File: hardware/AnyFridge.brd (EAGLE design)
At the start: 75.9 x 69.8 mm, 11 parts

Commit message: Minor updates.
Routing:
- net RX1: track 57.2 -> 56.4 mm
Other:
- board text added: "Designed by: AnyFridge Team Ethan Anderson, Isac Fletcher, Caden Allen"
- board text removed: "Designed by: Ethan Anderson, Isaac Fletcher, Caden Allen"
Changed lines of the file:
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@@
 <text x="5.08" y="46.99" size="1.778" layer="21">RGB LED</text>
 <text x="63.5" y="53.34" size="1.778" layer="21">Mode Toggle</text>
-<text x="5.08" y="36.83" size="1.778" layer="21" rot="SR270">Designed by:
+<text x="10.16" y="29.21" size="1.524" layer="21" rot="SR270" align="center">Designed by:
+AnyFridge Team
 Ethan Anderson,
-Isaac Fletcher,
+Isac Fletcher,
 Caden Allen</text>
 <text x="54.61" y="60.96" size="1.778" layer="21" rot="R270">R1</text>
@@
 <attribute name="MF" value="Vishay" x="35.56" y="-148.59" size="1.778" layer="27" display="off"/>
 <attribute name="MP" value="TSSP77038TT" x="35.56" y="-148.59" size="1.778" layer="27" display="off"/>
+<attribute name="NAME" x="12.64" y="5.83" size="1" layer="25" ratio="20" rot="SR0"/>
 <attribute name="NAME" x="12.64" y="5.83" size="1" layer="51" ratio="21" rot="SR0"/>
-<attribute name="NAME" x="12.64" y="5.83" size="1" layer="25" ratio="20" rot="SR0"/>
 <attribute name="PACKAGE" value="None" x="35.56" y="-148.59" size="1.778" layer="27" display="off"/>
 <attribute name="PRICE" value="None" x="35.56" y="-148.59" size="1.778" layer="27" display="off"/>
@@
 <contactref element="SCAN-1" pad="TX"/>
 <wire x1="49.53" y1="35.56" x2="44.45" y2="40.64" width="0.4064" layer="1"/>
-<wire x1="44.45" y1="49.53" x2="44.45" y2="40.64" width="0.4064" layer="1"/>
-<wire x1="44.45" y1="49.53" x2="40.64" y2="49.53" width="0.4064" layer="1"/>
+<wire x1="44.45" y1="40.64" x2="44.45" y2="48.26" width="0.4064" layer="1"/>
+<wire x1="44.45" y1="48.26" x2="43.18" y2="49.53" width="0.4064" layer="1"/>
+<wire x1="43.18" y1="49.53" x2="40.64" y2="49.53" width="0.4064" layer="1"/>
 <contactref element="TP_RX" pad="TP"/>
 <wire x1="13.11185" y1="62.23" x2="11.84185" y2="63.5" width="0.4064" layer="16"/>

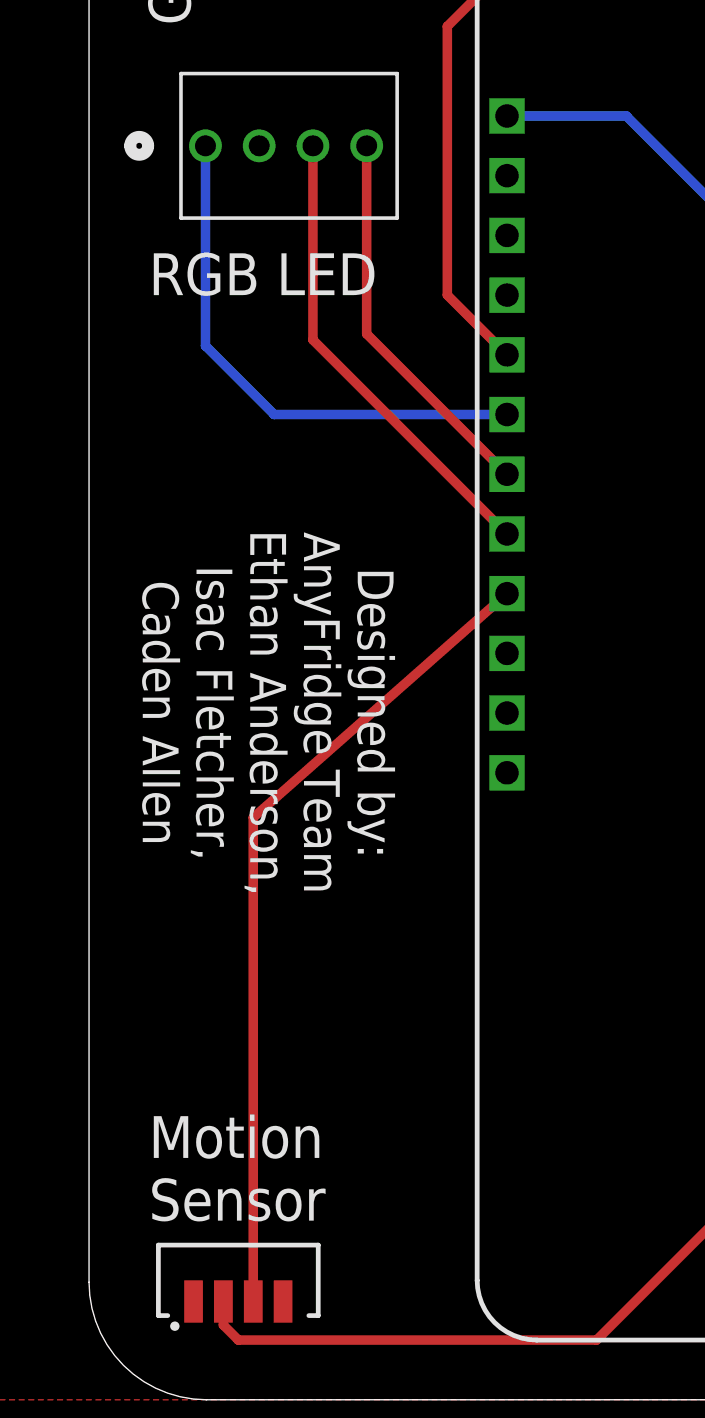
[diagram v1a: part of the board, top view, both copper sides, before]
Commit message: Added 120 ohm resistor to board/schematic
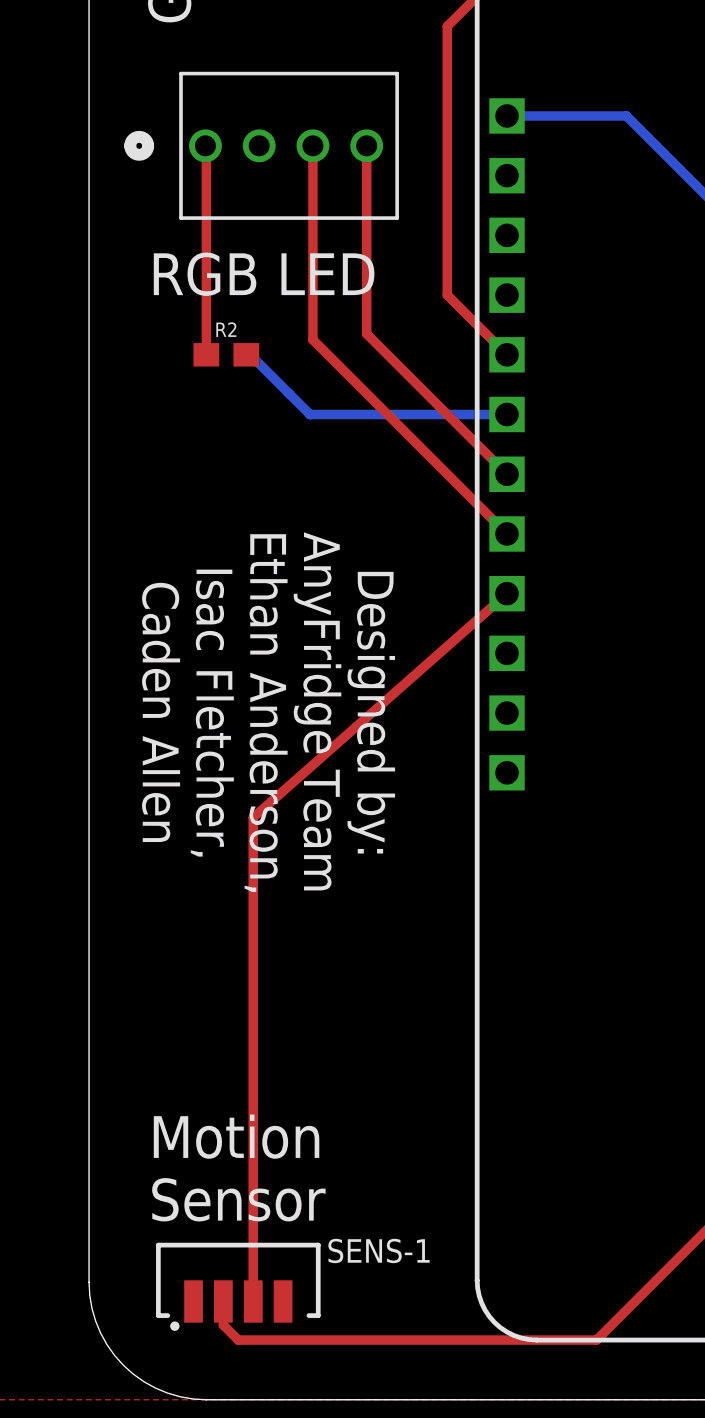
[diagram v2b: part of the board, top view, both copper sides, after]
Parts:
- added R2: 120OHM, SparkFun-Resistors:0603
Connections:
- removed net RED: ESP-1.33, LED-1.1
- new net RED-IN: ESP-1.33, R2.2
- new net RED-OUT: LED-1.1, R2.1
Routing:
- net RED: track 22.5 -> 0.00 mm
- net RED-IN: track 0.00 -> 12.5 mm
- net RED-OUT: track 0.00 -> 8.91 mm
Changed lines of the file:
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@@
 <layer number="154" name="FabDoc2" color="7" fill="1" visible="no" active="no"/>
 <layer number="155" name="FabDoc3" color="7" fill="1" visible="no" active="no"/>
+<layer number="156" name="gesam-Maß" color="1" fill="7" visible="no" active="no"/>
+<layer number="157" name="FaceMchng" color="3" fill="1" visible="no" active="no"/>
+<layer number="158" name="FaceMMeas" color="3" fill="1" visible="no" active="no"/>
+<layer number="159" name="Geh-Bear2" color="1" fill="7" visible="no" active="no"/>
+<layer number="160" name="Topologie" color="9" fill="1" visible="no" active="no"/>
+<layer number="161" name="tomplace2" color="7" fill="1" visible="no" active="no"/>
 <layer number="166" name="AntennaArea" color="7" fill="1" visible="no" active="no"/>
 <layer number="168" name="4mmHeightArea" color="7" fill="1" visible="no" active="no"/>
@@
 <layer number="250" name="Descript" color="3" fill="1" visible="no" active="no"/>
 <layer number="251" name="SMDround" color="12" fill="11" visible="no" active="no"/>
+<layer number="252" name="BR-BS" color="7" fill="1" visible="no" active="no"/>
 <layer number="253" name="Extra" color="7" fill="1" visible="no" active="no"/>
 <layer number="254" name="cooling" color="7" fill="1" visible="no" active="no"/>
@@
 <attribute name="MF" value="Vishay" x="35.56" y="-148.59" size="1.778" layer="27" display="off"/>
 <attribute name="MP" value="TSSP77038TT" x="35.56" y="-148.59" size="1.778" layer="27" display="off"/>
+<attribute name="NAME" x="12.64" y="5.83" size="1" layer="51" ratio="21" rot="SR0"/>
 <attribute name="NAME" x="12.64" y="5.83" size="1" layer="25" ratio="20" rot="SR0"/>
-<attribute name="NAME" x="12.64" y="5.83" size="1" layer="51" ratio="21" rot="SR0"/>
 <attribute name="PACKAGE" value="None" x="35.56" y="-148.59" size="1.778" layer="27" display="off"/>
 <attribute name="PRICE" value="None" x="35.56" y="-148.59" size="1.778" layer="27" display="off"/>
@@
 <attribute name="TP_SIGNAL_NAME" value="" x="13.97" y="66.04" size="1.778" layer="27" rot="R90" display="off"/>
 <attribute name="VALUE" x="10.16" y="64.77" size="0.0254" layer="27" rot="R90"/>
+</element>
+<element name="R2" library="SparkFun-Resistors" package="0603" value="120OHM" x="8.382" y="44.45" smashed="yes">
+<attribute name="NAME" x="8.382" y="45.212" size="0.6096" layer="25" font="vector" ratio="20" align="bottom-center"/>
+<attribute name="VALUE" x="8.382" y="43.688" size="0.6096" layer="27" font="vector" ratio="20" align="top-center"/>
 </element>
 </elements>
@@
 <wire x1="30.48" y1="20.32" x2="30.48" y2="49.53" width="0.4064" layer="16"/>
 </signal>
-<signal name="RED">
-<contactref element="LED-1" pad="1"/>
+<signal name="RED-IN">
 <contactref element="ESP-1" pad="33"/>
-<wire x1="10.414" y1="41.91" x2="20.32" y2="41.91" width="0.4064" layer="16"/>
-<wire x1="7.493" y1="44.831" x2="10.414" y2="41.91" width="0.4064" layer="16"/>
-<wire x1="7.493" y1="53.34" x2="7.493" y2="44.831" width="0.4064" layer="16"/>
+<wire x1="20.32" y1="41.91" x2="11.938" y2="41.91" width="0.4064" layer="16"/>
+<wire x1="11.938" y1="41.91" x2="11.049" y2="42.799" width="0.4064" layer="16"/>
+<contactref element="R2" pad="2"/>
+<wire x1="11.049" y1="42.799" x2="9.398" y2="44.45" width="0.4064" layer="16"/>
+<wire x1="9.398" y1="44.45" x2="8.89" y2="44.45" width="0.4064" layer="16"/>
+<wire x1="8.89" y1="44.45" x2="9.232" y2="44.45" width="0" layer="19" extent="1-16"/>
 </signal>
 <signal name="BLUE">
@@
 <wire x1="9.525" y1="24.765" x2="9.525" y2="4.18" width="0.4064" layer="1"/>
 </signal>
+<signal name="RED-OUT">
+<contactref element="LED-1" pad="1"/>
+<contactref element="R2" pad="1"/>
+<wire x1="7.532" y1="44.45" x2="7.532" y2="53.301" width="0.4064" layer="1"/>
+<wire x1="7.532" y1="53.301" x2="7.493" y2="53.34" width="0.4064" layer="1"/>
+</signal>
 </signals>

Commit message: schematic updated
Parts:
- R2: value 120OHM -> 68OHM-0603-1/10W-1%
- moved R2 0.76 mm to (7.62, 44.5)
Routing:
- net RED-IN: track 12.5 -> 12.9 mm, vias 0 -> 1
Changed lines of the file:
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@@
 <attribute name="VALUE" x="10.16" y="64.77" size="0.0254" layer="27" rot="R90"/>
 </element>
-<element name="R2" library="SparkFun-Resistors" package="0603" value="120OHM" x="8.382" y="44.45" smashed="yes">
-<attribute name="NAME" x="8.382" y="45.212" size="0.6096" layer="25" font="vector" ratio="20" align="bottom-center"/>
-<attribute name="VALUE" x="8.382" y="43.688" size="0.6096" layer="27" font="vector" ratio="20" align="top-center"/>
+<element name="R2" library="SparkFun-Resistors" package="0603" value="68OHM-0603-1/10W-1%" x="7.62" y="44.45" smashed="yes">
+<attribute name="NAME" x="7.62" y="45.212" size="0.6096" layer="25" font="vector" ratio="20" align="bottom-center"/>
+<attribute name="VALUE" x="7.62" y="43.688" size="0.6096" layer="27" font="vector" ratio="20" align="top-center"/>
 </element>
 </elements>
@@
 <contactref element="ESP-1" pad="33"/>
 <wire x1="20.32" y1="41.91" x2="11.938" y2="41.91" width="0.4064" layer="16"/>
-<wire x1="11.938" y1="41.91" x2="11.049" y2="42.799" width="0.4064" layer="16"/>
 <contactref element="R2" pad="2"/>
-<wire x1="11.049" y1="42.799" x2="9.398" y2="44.45" width="0.4064" layer="16"/>
-<wire x1="9.398" y1="44.45" x2="8.89" y2="44.45" width="0.4064" layer="16"/>
-<wire x1="8.89" y1="44.45" x2="9.232" y2="44.45" width="0" layer="19" extent="1-16"/>
+<via x="11.938" y="41.91" extent="1-16" drill="0.35"/>
+<wire x1="11.938" y1="41.91" x2="9.398" y2="44.45" width="0.4064" layer="1"/>
+<wire x1="9.398" y1="44.45" x2="8.47" y2="44.45" width="0.4064" layer="1"/>
 </signal>
 <signal name="BLUE">
@@
 <contactref element="LED-1" pad="1"/>
 <contactref element="R2" pad="1"/>
-<wire x1="7.532" y1="44.45" x2="7.532" y2="53.301" width="0.4064" layer="1"/>
-<wire x1="7.532" y1="53.301" x2="7.493" y2="53.34" width="0.4064" layer="1"/>
+<wire x1="6.77" y1="44.45" x2="6.77" y2="52.617" width="0.4064" layer="1"/>
+<wire x1="6.77" y1="52.617" x2="7.493" y2="53.34" width="0.4064" layer="1"/>
 </signal>
 </signals>

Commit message: Add Green and Blue resistors
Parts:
- added R3, R4: 22Ω, SparkFun-Resistors:0603
- moved R2 1.27 mm to (6.35, 44.5), turned to 270 degrees
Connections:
- net RED-IN renamed RED
- new net N$2: LED-1.4, R3.1
- new net N$3: LED-1.3, R4.1
- net BLUE: now also R4.2; no longer LED-1.3
- net GREEN: now also R3.2; no longer LED-1.4
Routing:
- net N$3: track 0.00 -> 8.83 mm
- net GREEN: track 16.4 -> 8.10 mm
- net N$2: track 0.00 -> 8.20 mm
- net BLUE: track 19.9 -> 14.7 mm
- net RED: track 12.9 -> 15.7 mm
- net RED-OUT: track 9.19 -> 8.51 mm
- net 3.3V: track 152.1 -> 152.6 mm
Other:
- board text added: "AnyFridge V1.0"
- board text added: "Designed by: Ethan Anderson, Isac Fletcher, Caden Allen"
- board text removed: "Designed by: AnyFridge Team Ethan Anderson, Isac Fletcher, Caden Allen"

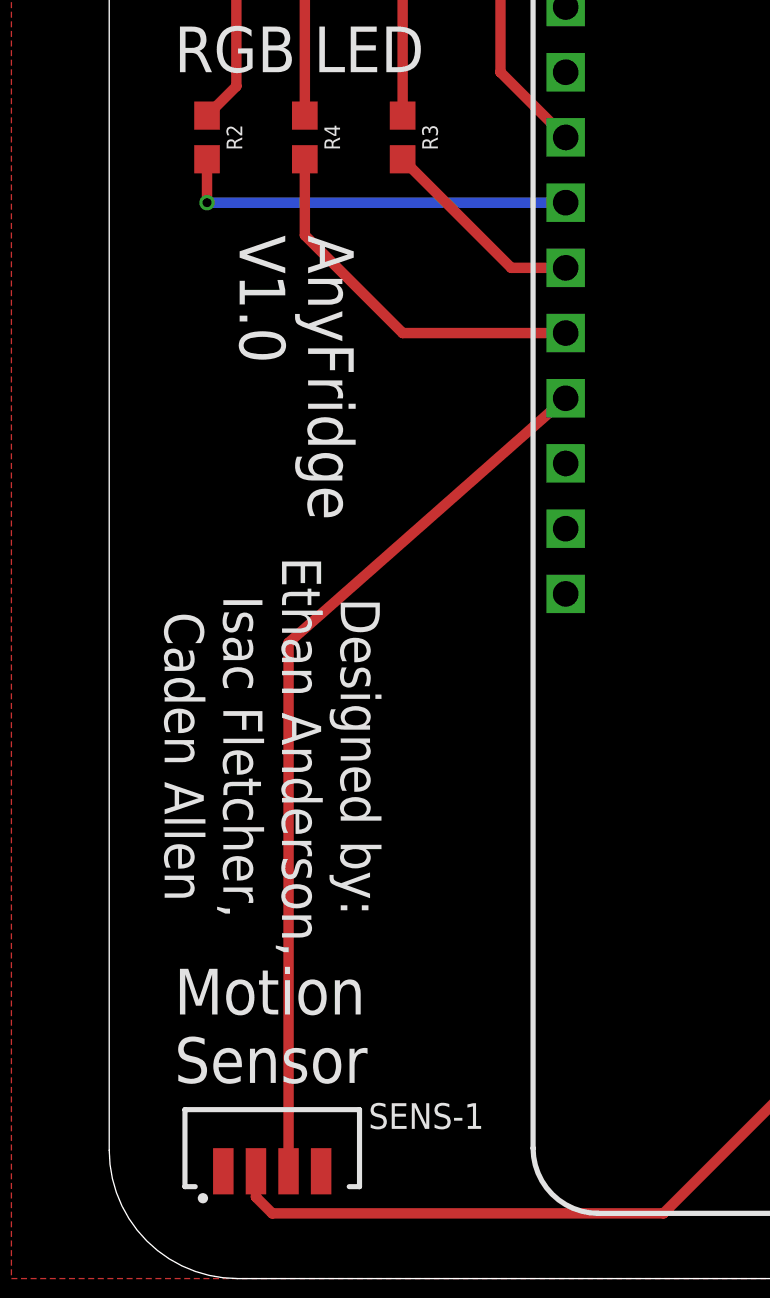
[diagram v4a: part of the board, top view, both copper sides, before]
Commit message: Put project name + revision in silkscreen, rename resistor to LED pins
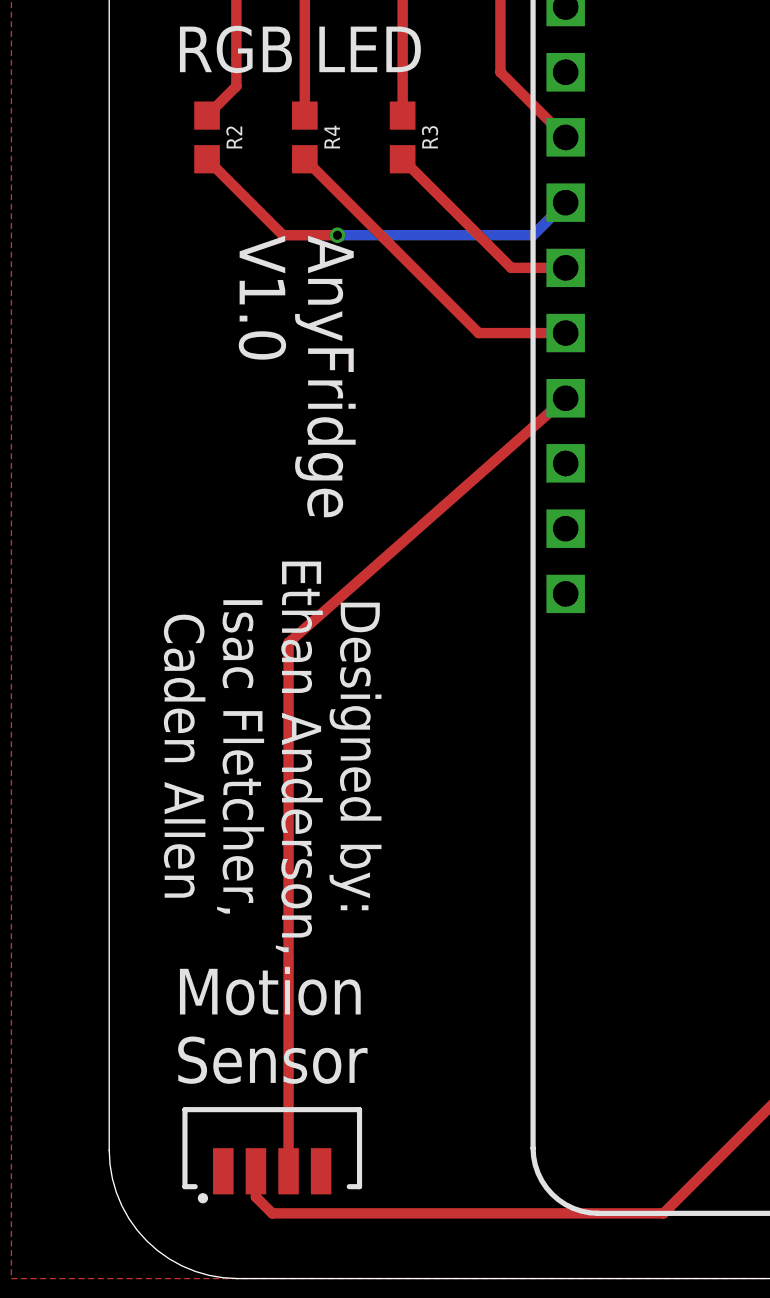
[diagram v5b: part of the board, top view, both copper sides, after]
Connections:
- net N$2 renamed GREEN-IN
- net N$3 renamed BLUE-IN
- net RED-OUT renamed RED-IN
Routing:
- net BLUE: track 14.7 -> 13.0 mm
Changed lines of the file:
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@@
 <attribute name="MF" value="Vishay" x="35.56" y="-148.59" size="1.778" layer="27" display="off"/>
 <attribute name="MP" value="TSSP77038TT" x="35.56" y="-148.59" size="1.778" layer="27" display="off"/>
+<attribute name="NAME" x="12.64" y="5.83" size="1" layer="25" ratio="20" rot="SR0"/>
 <attribute name="NAME" x="12.64" y="5.83" size="1" layer="51" ratio="21" rot="SR0"/>
-<attribute name="NAME" x="12.64" y="5.83" size="1" layer="25" ratio="20" rot="SR0"/>
 <attribute name="PACKAGE" value="None" x="35.56" y="-148.59" size="1.778" layer="27" display="off"/>
 <attribute name="PRICE" value="None" x="35.56" y="-148.59" size="1.778" layer="27" display="off"/>
@@
 <contactref element="ESP-1" pad="12"/>
 <contactref element="R4" pad="2"/>
-<wire x1="10.16" y1="43.6" x2="10.16" y2="40.64" width="0.4064" layer="1"/>
-<wire x1="10.16" y1="40.64" x2="13.97" y2="36.83" width="0.4064" layer="1"/>
-<wire x1="13.97" y1="36.83" x2="20.32" y2="36.83" width="0.4064" layer="1"/>
+<wire x1="10.16" y1="43.6" x2="16.93" y2="36.83" width="0.4064" layer="1"/>
+<wire x1="16.93" y1="36.83" x2="20.32" y2="36.83" width="0.4064" layer="1"/>
 </signal>
 <signal name="GREEN">
@@
 <wire x1="9.525" y1="24.765" x2="9.525" y2="4.18" width="0.4064" layer="1"/>
 </signal>
-<signal name="RED-OUT">
+<signal name="RED-IN">
 <contactref element="LED-1" pad="1"/>
 <contactref element="R2" pad="1"/>
@@
 <contactref element="R2" pad="2"/>
 <contactref element="ESP-1" pad="33"/>
-<wire x1="6.35" y1="43.6" x2="6.35" y2="41.91" width="0.4064" layer="1"/>
-<via x="6.35" y="41.91" extent="1-16" drill="0.35"/>
-<wire x1="20.32" y1="41.91" x2="6.35" y2="41.91" width="0.4064" layer="16"/>
-</signal>
-<signal name="N$2">
+<wire x1="11.43" y1="40.64" x2="9.31" y2="40.64" width="0.4064" layer="1"/>
+<wire x1="6.35" y1="43.6" x2="9.31" y2="40.64" width="0.4064" layer="1"/>
+<via x="11.43" y="40.64" extent="1-16" drill="0.35"/>
+<wire x1="19.05" y1="40.64" x2="20.32" y2="41.91" width="0.4064" layer="16"/>
+<wire x1="11.43" y1="40.64" x2="19.05" y2="40.64" width="0.4064" layer="16"/>
+</signal>
+<signal name="GREEN-IN">
 <contactref element="LED-1" pad="4"/>
 <contactref element="R3" pad="1"/>
@@
 <wire x1="13.97" y1="52.959" x2="14.351" y2="53.34" width="0.1524" layer="1"/>
 </signal>
-<signal name="N$3">
+<signal name="BLUE-IN">
 <contactref element="LED-1" pad="3"/>
 <contactref element="R4" pad="1"/>
